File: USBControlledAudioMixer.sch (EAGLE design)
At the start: 50 parts, among them IC1 TDA7448, IC2 TS912, IC3 MEGA8-AI, J2 AVR_SPI_PRG_6NS, Q1 16MHz, U1 LMR62014

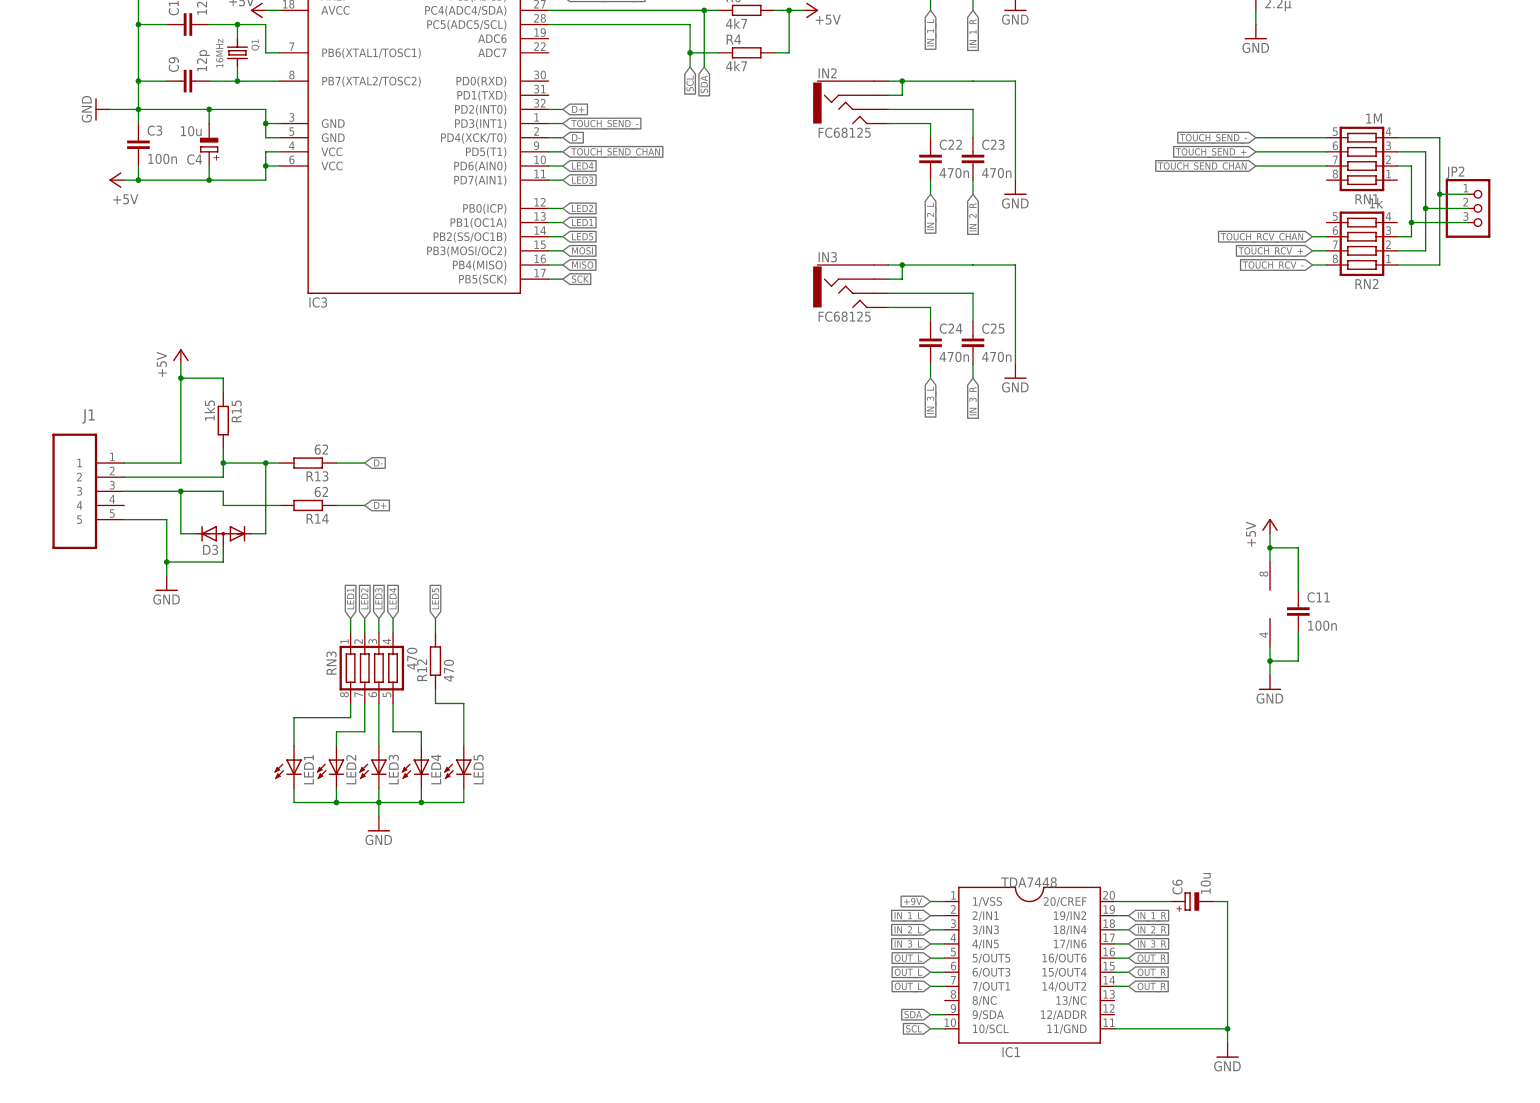
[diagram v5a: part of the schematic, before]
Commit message: Semi-finalized board, front and back panel Added 100nF capacitor for the TDA7448 mixer
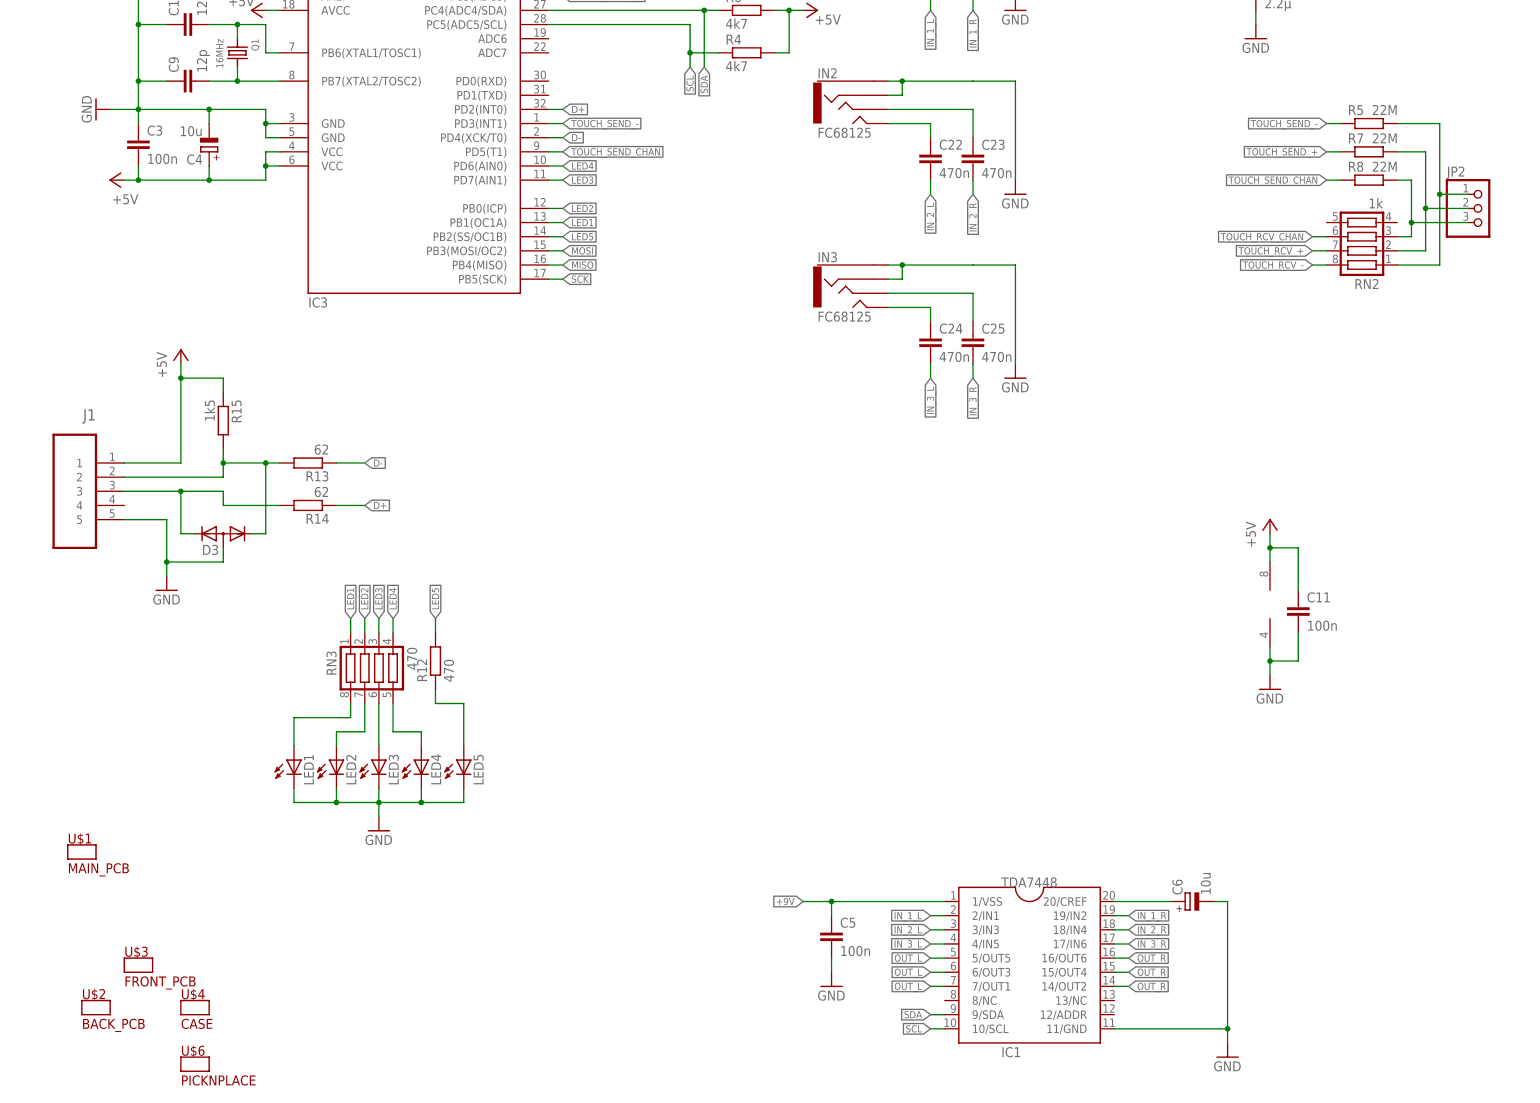
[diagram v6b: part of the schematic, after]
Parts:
- removed RN1: 1M, Simplex-rlc:RES_ARR
- added C5: 100n, rcl:C-EUC0603
- added R5, R7, R8: 22M, rcl:R-EU_R0603
- C20, C21, C22, C23, C24, C25, C26, C27: OC_DIGIKEY (none) -> 338-2776-1-ND; OC_TME MKS02-470N/63 -> (none); PRICE_100 0.19 -> 0.487
- C9: OC_DIGIKEY (none) -> 1276-1254-1-ND; OC_TME CL21C220JBANNNC -> (none); PRICE_100 (none) -> 0.126
- IC1: OC_DIGIKEY (none) -> 497-8884-1-ND; PRICE_100 (none) -> 2.35
- IC2: OC_DIGIKEY (none) -> 497-6618-1-ND; PRICE_100 (none) -> 0.654
- IC3: PRICE_10 1.37 -> (none); PRICE_100 (none) -> 1.04
- IN1, IN2, IN3, U$5: PRICE_100 (none) -> 0.313
- J1: OC_DIGIKEY (none) -> WM17141CT-ND; PRICE_100 (none) -> 0.74
- JP2: OC_DIGIKEY (none) -> WM4101-ND; PRICE_100 (none) -> 0.227
- Q1: PRICE_10 0.53 -> (none); PRICE_100 (none) -> 0.415
- R10: OC_DIGIKEY (none) -> RHM10KCGCT-ND; OC_TME SMD0805-10K -> (none); PRICE_100 (none) -> 0.0042
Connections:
- net +9V: now also C5.1
- net GND: now also C5.2
- net N$18: now also R5.2; no longer RN1.4
- net N$19: now also R7.2; no longer RN1.3
- net N$20: now also R8.2; no longer RN1.2
- net TOUCH_SEND_+: now also R7.1; no longer RN1.6
- net TOUCH_SEND_-: now also R5.1; no longer RN1.5
- net TOUCH_SEND_CHAN: now also R8.1; no longer RN1.7

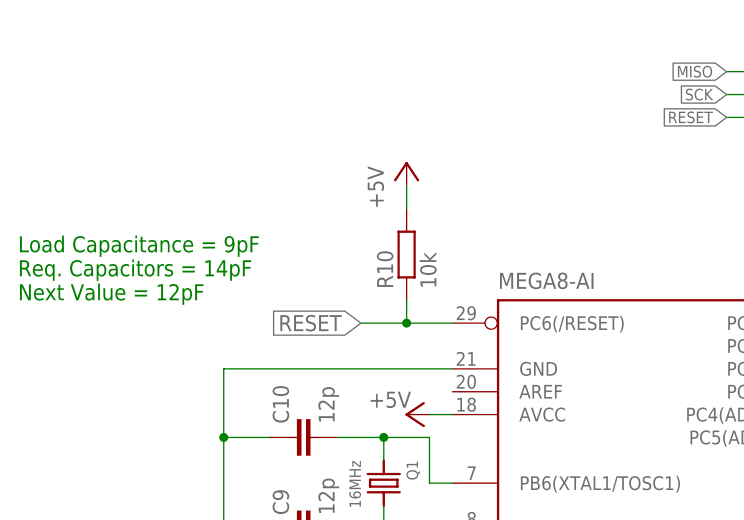
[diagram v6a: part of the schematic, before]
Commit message: Added ESD protection for the RESET line
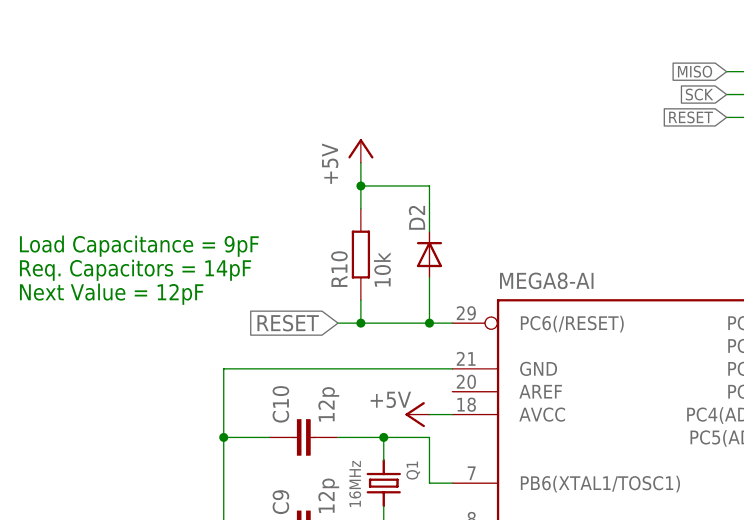
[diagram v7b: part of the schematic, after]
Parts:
- added D2: (no value), diode:DIODE-SOD323-R
- C9: PRICE_100 0.126 -> 0.013
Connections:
- net +5V: now also D2.C
- net RESET: now also D2.A
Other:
- moved on the sheet: R10
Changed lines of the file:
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@@
 <?xml version="1.0" encoding="utf-8"?>
 <!DOCTYPE eagle SYSTEM "eagle.dtd">
-<eagle version="6.6.0">
+<eagle version="6.5.0">
 <drawing>
 <settings>
@@
 <part name="C9" library="rcl" deviceset="C-EU" device="C0603" value="12p">
 <attribute name="OC_DIGIKEY" value="1276-1254-1-ND"/>
-<attribute name="PRICE_100" value="0.126"/>
+<attribute name="PRICE_100" value="0.013"/>
 </part>
 <part name="R10" library="rcl" deviceset="R-EU_" device="R0603" value="10k">
@@
 </part>
 <part name="GND12" library="supply1" deviceset="GND" device=""/>
+<part name="D2" library="diode" deviceset="DIODE-" device="SOD323-R">
+<attribute name="OC_DIGIKEY" value="497-10893-1-ND"/>
+<attribute name="PRICE_100" value="0.092"/>
+</part>
 </parts>
 <sheets>
@@
 <attribute name="PRICE_100" x="38.1" y="195.58" size="1.27" layer="96" rot="R90" display="off"/>
 </instance>
-<instance part="R10" gate="G$1" x="50.8" y="226.06" rot="R90">
-<attribute name="OC_DIGIKEY" x="50.8" y="226.06" size="1.778" layer="96" rot="R90" display="off"/>
-<attribute name="PRICE_100" x="50.8" y="226.06" size="1.27" layer="96" rot="R90" display="off"/>
+<instance part="R10" gate="G$1" x="45.72" y="226.06" rot="R90">
+<attribute name="OC_DIGIKEY" x="45.72" y="226.06" size="1.778" layer="96" rot="R90" display="off"/>
+<attribute name="PRICE_100" x="45.72" y="226.06" size="1.27" layer="96" rot="R90" display="off"/>
 </instance>
 <instance part="C3" gate="G$1" x="30.48" y="185.42">
@@
 <attribute name="PRICE_100" x="78.74" y="193.04" size="1.778" layer="96" display="off"/>
 </instance>
-<instance part="P+2" gate="1" x="50.8" y="236.22"/>
+<instance part="P+2" gate="1" x="45.72" y="238.76"/>
 <instance part="GND2" gate="1" x="226.06" y="20.32"/>
 <instance part="LED4" gate="G$1" x="81.28" y="73.66">
@@
 </instance>
 <instance part="GND12" gate="1" x="154.94" y="33.02"/>
+<instance part="D2" gate="G$1" x="53.34" y="226.06" rot="R90">
+<attribute name="OC_DIGIKEY" x="53.34" y="226.06" size="1.778" layer="96" rot="R90" display="off"/>
+<attribute name="PRICE_100" x="53.34" y="226.06" size="1.778" layer="96" rot="R90" display="off"/>
+</instance>
 </instances>
 <busses>
@@
 <segment>
 <pinref part="R10" gate="G$1" pin="2"/>
-<wire x1="50.8" y1="231.14" x2="50.8" y2="233.68" width="0.1524" layer="91"/>
+<wire x1="45.72" y1="231.14" x2="45.72" y2="233.68" width="0.1524" layer="91"/>
 <pinref part="P+2" gate="1" pin="+5V"/>
+<pinref part="D2" gate="G$1" pin="C"/>
+<wire x1="45.72" y1="233.68" x2="45.72" y2="236.22" width="0.1524" layer="91"/>
+<wire x1="53.34" y1="228.6" x2="53.34" y2="233.68" width="0.1524" layer="91"/>
+<wire x1="53.34" y1="233.68" x2="45.72" y2="233.68" width="0.1524" layer="91"/>
+<junction x="45.72" y="233.68"/>
 </segment>
 <segment>
@@
 <pinref part="IC3" gate="G$1" pin="PC6(/RESET)"/>
 <pinref part="R10" gate="G$1" pin="1"/>
-<wire x1="55.88" y1="218.44" x2="50.8" y2="218.44" width="0.1524" layer="91"/>
-<wire x1="50.8" y1="218.44" x2="50.8" y2="220.98" width="0.1524" layer="91"/>
-<wire x1="50.8" y1="218.44" x2="45.72" y2="218.44" width="0.1524" layer="91"/>
-<junction x="50.8" y="218.44"/>
-<label x="45.72" y="218.44" size="1.778" layer="95" rot="R180" xref="yes"/>
+<wire x1="55.88" y1="218.44" x2="53.34" y2="218.44" width="0.1524" layer="91"/>
+<wire x1="53.34" y1="218.44" x2="45.72" y2="218.44" width="0.1524" layer="91"/>
+<wire x1="45.72" y1="218.44" x2="45.72" y2="220.98" width="0.1524" layer="91"/>
+<wire x1="45.72" y1="218.44" x2="43.18" y2="218.44" width="0.1524" layer="91"/>
+<junction x="45.72" y="218.44"/>
+<label x="43.18" y="218.44" size="1.778" layer="95" rot="R180" xref="yes"/>
+<pinref part="D2" gate="G$1" pin="A"/>
+<wire x1="53.34" y1="223.52" x2="53.34" y2="218.44" width="0.1524" layer="91"/>
+<junction x="53.34" y="218.44"/>
 </segment>
 </net>

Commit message: Fixed hole size, use smaller connector for the front panel
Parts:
- JP2: OC_DIGIKEY WM4101-ND -> WM2734-ND
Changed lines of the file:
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@@
 <?xml version="1.0" encoding="utf-8"?>
 <!DOCTYPE eagle SYSTEM "eagle.dtd">
-<eagle version="6.5.0">
+<eagle version="6.6.0">
 <drawing>
 <settings>
@@
 </part>
 <part name="JP2" library="TinyMix3" deviceset="PINHD-1X3" device="">
-<attribute name="OC_DIGIKEY" value="WM4101-ND"/>
+<attribute name="OC_DIGIKEY" value="WM2734-ND"/>
 <attribute name="PRICE_100" value="0.227"/>
 </part>
